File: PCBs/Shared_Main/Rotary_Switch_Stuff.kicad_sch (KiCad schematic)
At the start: 11 parts, among them J2 Rotary switches pin 1, Q1 BC547, Q2 BC547, Q3 BC547, Q4 BC547, Q5 BC547, Q6 BC547, Q7 BC547, Q8 BC547

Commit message: shared main wip
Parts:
- J2: footprint (none) -> TerminalBlock_Phoenix:TerminalBlock_Phoenix_MPT-0,5-8-2.54_1x08_P2.54mm_Horizontal
- Q1, Q2, Q3, Q4, Q5, Q6, Q7, Q8: footprint (none) -> Package_TO_SOT_THT:TO-92_Inline
- R1: footprint (none) -> Resistor_THT:R_Axial_DIN0207_L6.3mm_D2.5mm_P7.62mm_Horizontal
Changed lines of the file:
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@@
 			)
 		)
-		(property "Footprint" ""
+		(property "Footprint" "Package_TO_SOT_THT:TO-92_Inline"
 			(at 110.49 92.71 0)
 			(hide yes)
@@
 			)
 		)
-		(property "Footprint" ""
+		(property "Footprint" "Package_TO_SOT_THT:TO-92_Inline"
 			(at 148.59 92.71 0)
 			(hide yes)
@@
 			)
 		)
-		(property "Footprint" ""
+		(property "Footprint" "Resistor_THT:R_Axial_DIN0207_L6.3mm_D2.5mm_P7.62mm_Horizontal"
 			(at 232.41 82.55 0)
 			(hide yes)
@@
 			)
 		)
-		(property "Footprint" ""
+		(property "Footprint" "Package_TO_SOT_THT:TO-92_Inline"
 			(at 186.69 92.71 0)
 			(hide yes)
@@
 			)
 		)
-		(property "Footprint" ""
+		(property "Footprint" "Package_TO_SOT_THT:TO-92_Inline"
 			(at 129.54 92.71 0)
 			(hide yes)
@@
 			)
 		)
-		(property "Footprint" ""
+		(property "Footprint" "Package_TO_SOT_THT:TO-92_Inline"
 			(at 224.79 92.71 0)
 			(hide yes)
@@
 			)
 		)
-		(property "Footprint" ""
+		(property "Footprint" "Package_TO_SOT_THT:TO-92_Inline"
 			(at 91.44 92.71 0)
 			(hide yes)
@@
 			)
 		)
-		(property "Footprint" ""
+		(property "Footprint" "Package_TO_SOT_THT:TO-92_Inline"
 			(at 205.74 92.71 0)
 			(hide yes)
@@
 			)
 		)
-		(property "Footprint" ""
+		(property "Footprint" "TerminalBlock_Phoenix:TerminalBlock_Phoenix_MPT-0,5-8-2.54_1x08_P2.54mm_Horizontal"
 			(at 240.03 109.22 0)
 			(hide yes)
@@
 			)
 		)
-		(property "Footprint" ""
+		(property "Footprint" "Package_TO_SOT_THT:TO-92_Inline"
 			(at 167.64 92.71 0)
 			(hide yes)

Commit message: wip
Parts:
- Q1, Q2, Q3, Q4, Q5, Q6, Q7, Q8: footprint Package_TO_SOT_THT:TO-92_Inline -> Package_TO_SOT_THT:TO-92_Inline_Wide
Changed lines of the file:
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@@
 			)
 		)
-		(property "Footprint" "Package_TO_SOT_THT:TO-92_Inline"
+		(property "Footprint" "Package_TO_SOT_THT:TO-92_Inline_Wide"
 			(at 110.49 92.71 0)
 			(hide yes)
@@
 			)
 		)
-		(property "Footprint" "Package_TO_SOT_THT:TO-92_Inline"
+		(property "Footprint" "Package_TO_SOT_THT:TO-92_Inline_Wide"
 			(at 148.59 92.71 0)
 			(hide yes)
@@
 			)
 		)
-		(property "Footprint" "Package_TO_SOT_THT:TO-92_Inline"
+		(property "Footprint" "Package_TO_SOT_THT:TO-92_Inline_Wide"
 			(at 186.69 92.71 0)
 			(hide yes)
@@
 			)
 		)
-		(property "Footprint" "Package_TO_SOT_THT:TO-92_Inline"
+		(property "Footprint" "Package_TO_SOT_THT:TO-92_Inline_Wide"
 			(at 129.54 92.71 0)
 			(hide yes)
@@
 			)
 		)
-		(property "Footprint" "Package_TO_SOT_THT:TO-92_Inline"
+		(property "Footprint" "Package_TO_SOT_THT:TO-92_Inline_Wide"
 			(at 224.79 92.71 0)
 			(hide yes)
@@
 			)
 		)
-		(property "Footprint" "Package_TO_SOT_THT:TO-92_Inline"
+		(property "Footprint" "Package_TO_SOT_THT:TO-92_Inline_Wide"
 			(at 91.44 92.71 0)
 			(hide yes)
@@
 			)
 		)
-		(property "Footprint" "Package_TO_SOT_THT:TO-92_Inline"
+		(property "Footprint" "Package_TO_SOT_THT:TO-92_Inline_Wide"
 			(at 205.74 92.71 0)
 			(hide yes)
@@
 			)
 		)
-		(property "Footprint" "Package_TO_SOT_THT:TO-92_Inline"
+		(property "Footprint" "Package_TO_SOT_THT:TO-92_Inline_Wide"
 			(at 167.64 92.71 0)
 			(hide yes)

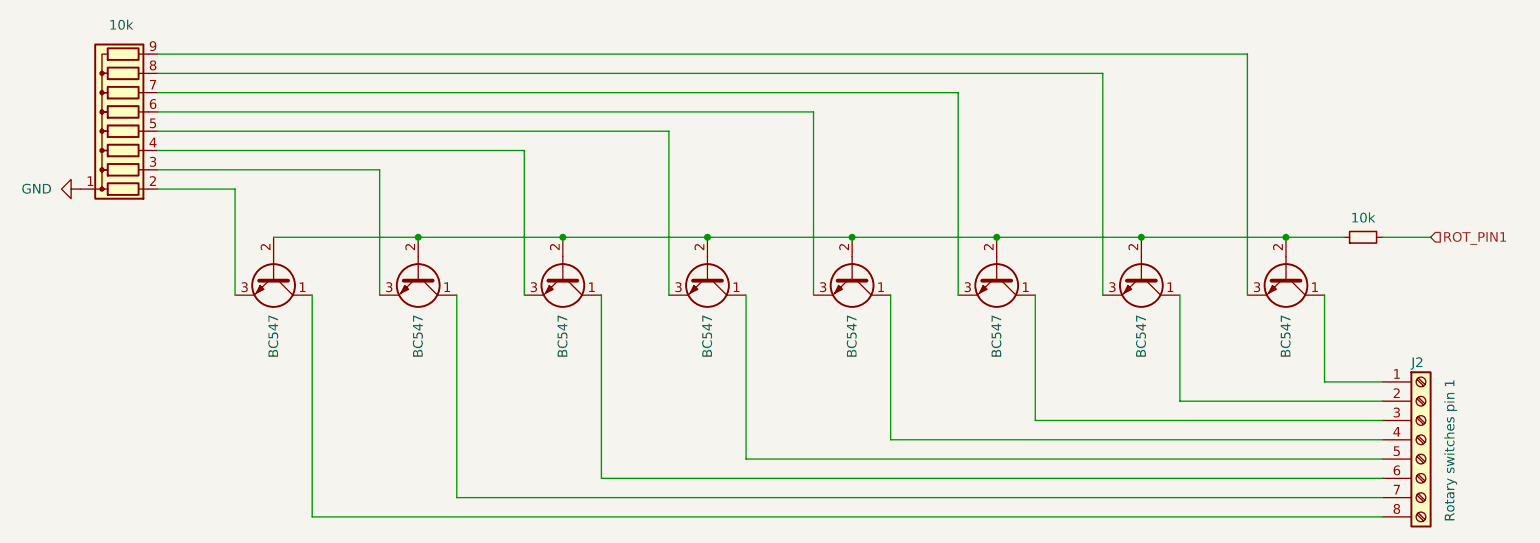
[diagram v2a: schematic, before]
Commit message: reduce to 4 rotary switch pin-1s
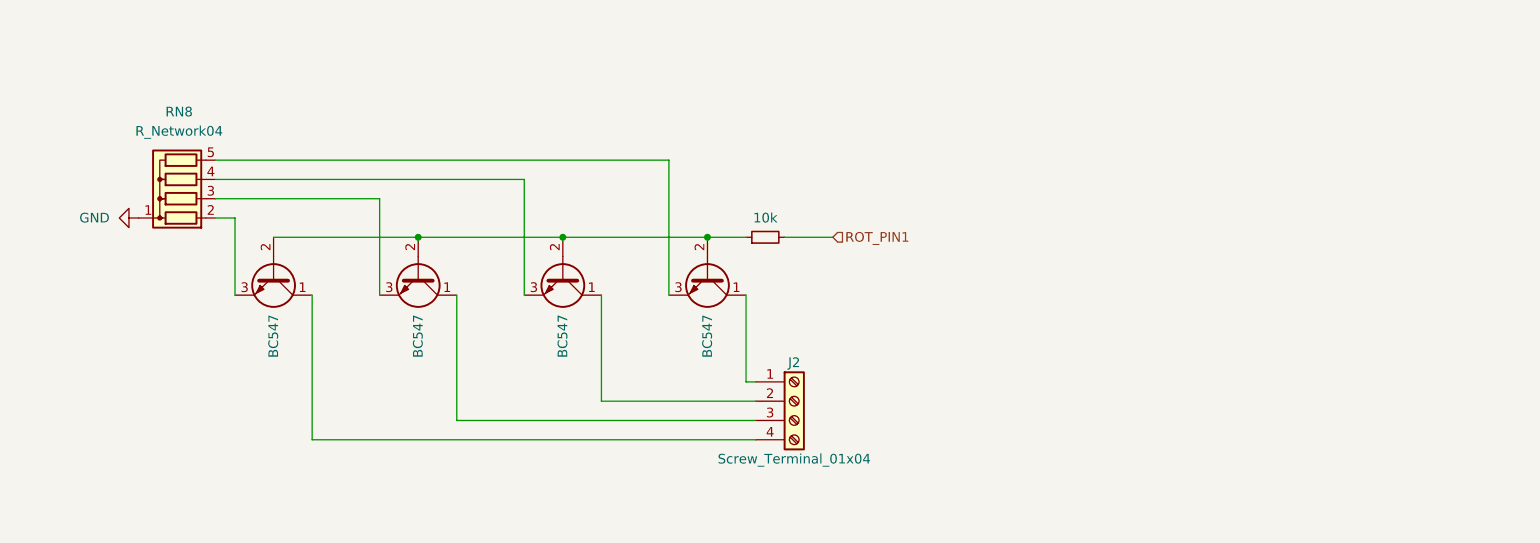
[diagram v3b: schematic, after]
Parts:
- removed Q5, Q6, Q7, Q8: BC547, Package_TO_SOT_THT:TO-92_Inline_Wide, symbol Transistor_BJT:Q_NPN_CBE
- J2: value Rotary switches pin 1 -> Screw_Terminal_01x04; footprint TerminalBlock_Phoenix:TerminalBlock_Phoenix_MPT-0,5-8-2.54_1x08_P2.54mm_Horizontal -> Custom_Footprints:SpringTerminal_1x04_P2.54mm_Vertical; symbol Connector:Screw_Terminal_01x08 -> Connector:Screw_Terminal_01x04
- RN8: value 10k -> R_Network04; footprint Resistor_THT:R_Array_SIP9 -> Resistor_THT:R_Array_SIP5; symbol Device:R_Network08 -> Device:R_Network04
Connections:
- net at Q2.1 (C): now also J2.3 (Pin_3); no longer J2.7 (Pin_7)
- net at Q4.1 (C): now also J2.1 (Pin_1); no longer J2.5 (Pin_5)
- net at Q3.1 (C): now also J2.2 (Pin_2); no longer J2.6 (Pin_6)
- net at Q1.1 (C): now also J2.4 (Pin_4); no longer J2.8 (Pin_8)

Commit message: revert to horizontal screw terminals to save cost
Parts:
- J2: value Screw_Terminal_01x04 -> GND or High-Z; footprint Custom_Footprints:SpringTerminal_1x04_P2.54mm_Vertical -> TerminalBlock_Phoenix:TerminalBlock_Phoenix_MPT-0,5-4-2.54_1x04_P2.54mm_Horizontal
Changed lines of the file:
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@@
 			)
 		)
-		(property "Value" "Screw_Terminal_01x04"
+		(property "Value" "GND or High-Z"
 			(at 157.48 111.76 0)
 			(show_name no)
@@
 			)
 		)
-		(property "Footprint" "Custom_Footprints:SpringTerminal_1x04_P2.54mm_Vertical"
+		(property "Footprint" "TerminalBlock_Phoenix:TerminalBlock_Phoenix_MPT-0,5-4-2.54_1x04_P2.54mm_Horizontal"
 			(at 157.48 104.14 0)
 			(hide yes)

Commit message: Fixed issues identified by Claude - batch 1
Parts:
- removed RN8: R_Network04, Resistor_THT:R_Array_SIP5, symbol Device:R_Network04
- added R7: 10k, Resistor_THT:R_Axial_DIN0207_L6.3mm_D2.5mm_P7.62mm_Horizontal, symbol Device:R_Small
- J2: value GND or High-Z -> GND or Floating
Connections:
- net GND: now also Q1.3 (E), Q2.3 (E), Q3.3 (E), Q4.3 (E), R7.2
- net at Q1.2 (B), Q2.2 (B), Q3.2 (B)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: now also R7.1
